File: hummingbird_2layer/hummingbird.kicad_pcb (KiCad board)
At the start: 4 copper layers, 53 x 20 mm, 47 parts, among them J1 USB_C_Receptacle_USB2.0_16P, J2 srv1, J3 srv2, J4 halleffect, J5 Conn_01x06, J6 Conn_01x02, J7 Conn_01x02, J8 PWR_IN, J9 Conn_02x02_Counter_Clockwise, Q1 AO3400A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

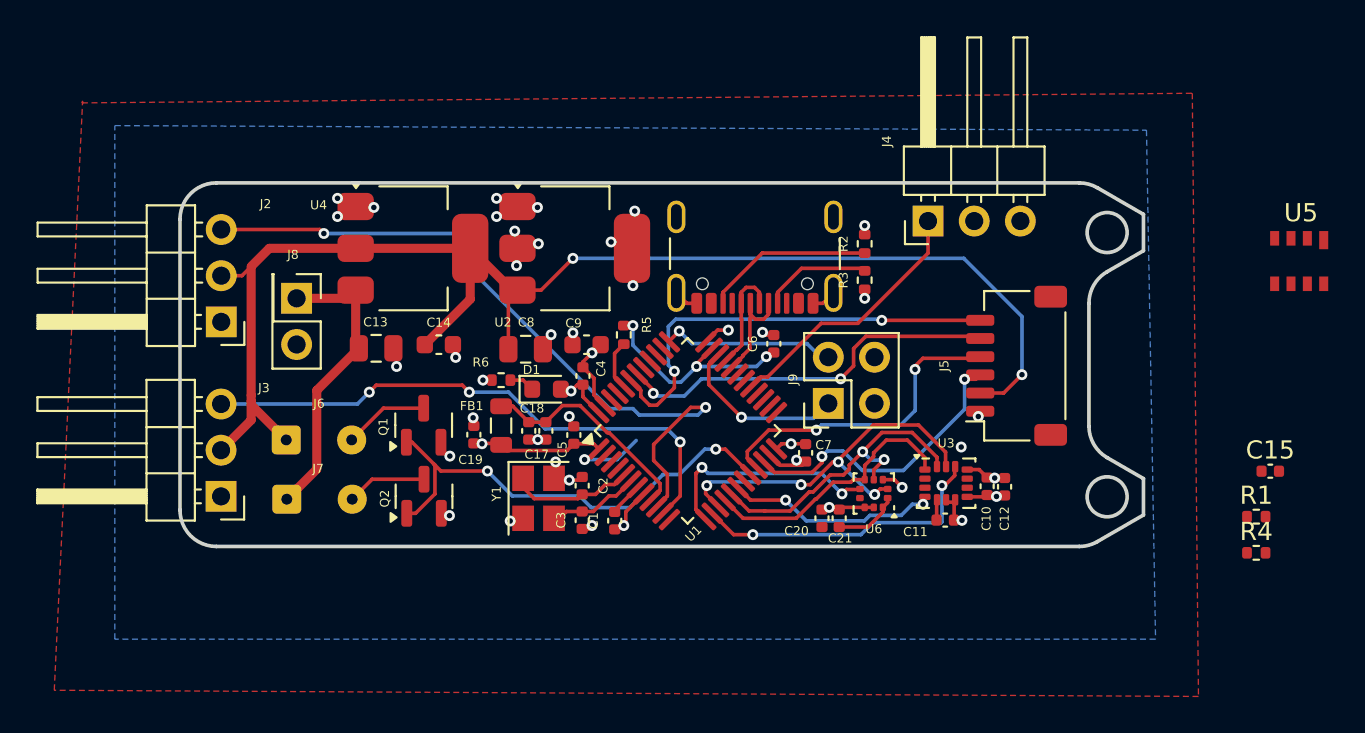
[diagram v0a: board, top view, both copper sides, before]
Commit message: backup before replacing sensor
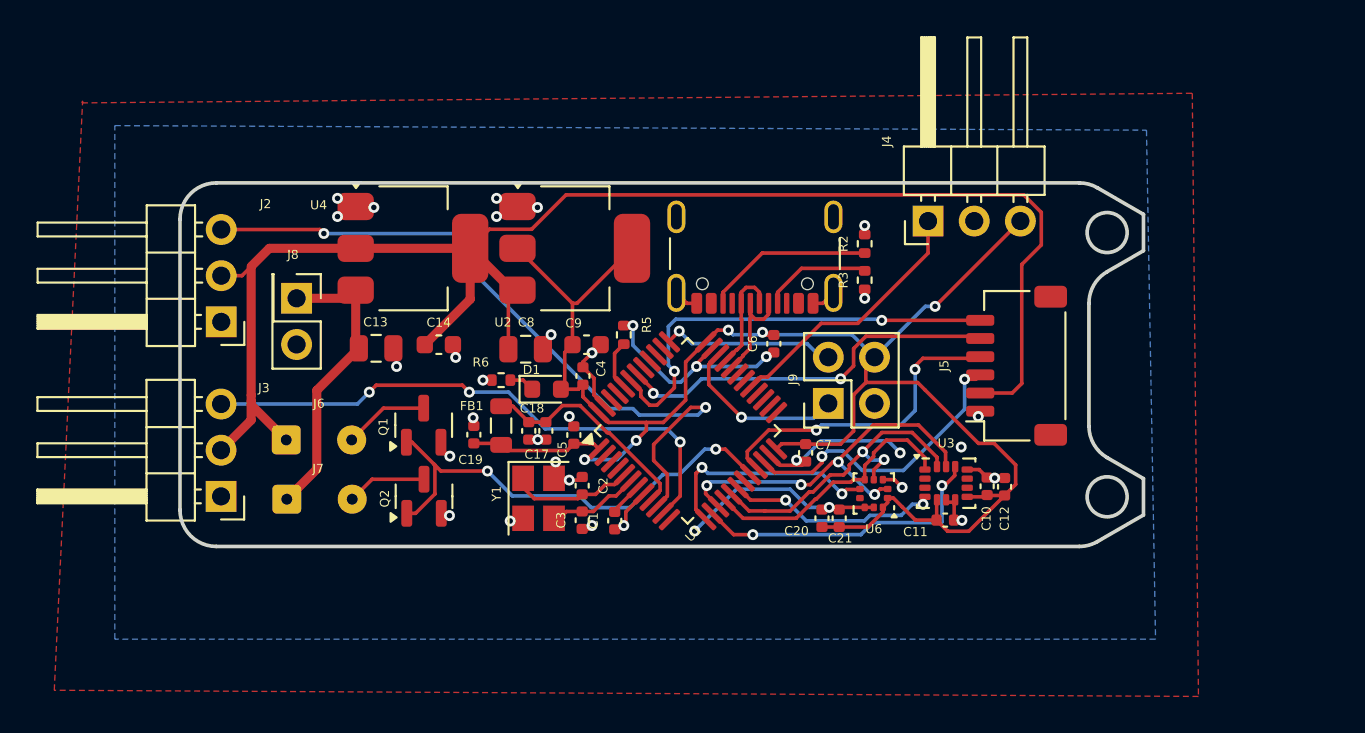
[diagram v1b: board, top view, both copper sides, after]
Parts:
- removed C15: 4u7, Capacitor_SMD:C_0402_1005Metric
- removed R1, R4: 10k, Resistor_SMD:R_0402_1005Metric
- removed U5: ~, custom:QFN (3.8x3.8)
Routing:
- net +3V3: track 23.8 -> 96.7 mm, vias 14 -> 5
- net GND: track 30.8 -> 45.7 mm, vias 33 -> 35
- net +5V: track 77.2 -> 86.9 mm, vias 2 -> 0
- removed copper zone on In1.Cu, net +3V3
- removed copper zone on In2.Cu, net GND
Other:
- copper layers 4 -> 2
